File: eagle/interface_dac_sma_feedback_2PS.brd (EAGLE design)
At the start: 119.6 x 108.5 mm, 37 parts, among them K1 G5V-2, X4 BU-SMA-V

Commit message: feedback on hv rails
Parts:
- removed C3, C5, C6: (no value), resistor:C050-055X075
- removed C7: (no value), rcl:C050-030X075
- removed CONTROLGD1, POWERGD: (no value), con-molex:KK-156-2
- removed D1, D10, D4, D9: P6KEXXA, diode:C1702-15
- removed D11: 1N4148DO35-10, diode:DO35-10
- removed D14, D2, D5, D6: 4742, diode:ZDIO-10
- removed D7, D8: 1N4004, diode:DO41-10
- removed GND, HV1, LV1, OUT: TPPAD1-20Y, testpad:P1-20Y
- removed K1: G5V-2, relay:G5V-2
- removed R10, R11: 1M, rcl:0207/12
- removed U$3: UCC27425, texas:DIL08
- removed U$5: VP0550, transistor-fet:TO92-
- removed U$7: DA-2320, trafo:DIL06
- removed X4: BU-SMA-V, con-coax:BU-SMA-V
- added CONTROLGD2: (no value), con-molex:KK-156-2
- added CONTROLHV, FDBACKHV, POWERINTERFACE: (no value), con-molex:KK-156-3
- added IC1: ISO1540, texas:DIL08
- added OK1: PS2501", optocoupler:DIL16
- added PCB1: ARDUINO_MICRO, E14_Arduino_published:ARDUINO_MICRO
- added R1, R2: 1.5k, resistor:0207/12
- added R14: 1k, resistor:0207/12
- added R16: (no value), pot:SP19L
- added R18: 100, rcl:0207/12
- added R6: 10k, resistor:0207/12
- added T1, T2, T3, T4: TIP122V, transistor-npn:TO220V
- added X1: BU-SMA-V, con-coax:BU-SMA-V
- C1: device resistor:C050-055X075 -> rcl:C050-050X075
- C2: value (none) -> 10n; device resistor:C050-055X075 -> resistor:C050-024X044
- C4: device resistor:C050-055X075 -> resistor:C075-063X106
- R4: value 1M -> 1k; device rcl:0207/12 -> resistor:0207/12
- R7: value 1M -> 40k; device rcl:0207/12 -> resistor:0207/12
- U$1: value DA-2320 -> LTC6992; device trafo:DIL06 -> linear-technology:DIL06
- U$2: value VN0550 -> MCP4728DIL; device transistor-fet:TO92- -> microchip:DIL10
- U$4: value VP0550 -> MAX9650DIL; device transistor-fet:TO92- -> maxim:DIL06-4
- U$6: value VN0550 -> MAX9650DIL; device transistor-fet:TO92- -> maxim:DIL06-4
- moved R4 94.9 mm to (5.59, 99.3), turned to 270 degrees
- moved U$4 73.7 mm to (17.4, 93.7)
- moved C4 71.4 mm to (98.3, 62.4)
- moved U$6 65.1 mm to (83.1, 94.4), turned to 270 degrees
- moved U$2 56.1 mm to (42.4, 76.5), turned to 0 degrees
- moved U$1 36.1 mm to (88.1, 73.2), turned to 270 degrees
- moved R7 33.1 mm to (68.2, 74.4), turned to 0 degrees
- moved C1 31.2 mm to (34.8, 63.5), turned to 180 degrees
- moved C2 28.6 mm to (72.0, 64.1), turned to 180 degrees
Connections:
- removed net +15V: C7.1, D11.C, K1.1, K1.8, K1.9, POWERGD.1, U$3.6
- removed net ENSW: CONTROLGD1.1, D11.A, K1.16
- removed net N$10: D8.C, LV1.TP
- removed net N$11: C1.2, D2.A, U$5.2
- removed net N$22: C2.1, U$7.2
- removed net N$23: C6.1, U$7.3
- removed net N$25: C2.2, D6.C, U$2.2
- removed net N$27: C6.2, D14.C, U$6.2
- removed net N$29: D7.A, HV1.TP
- removed net N$30: D14.A, D4.A, D8.A, R11.1, U$6.3, U$7.4
- removed net N$6: C4.2, U$7.1
- removed net N$9: U$7.5
- new net +12V: POWERINTERFACE.1, T1.2, T2.2, T3.2, T4.2, U$4.6, U$6.6
- new net A+5: IC1.1, PCB1.+5V
- new net AGND: IC1.4, PCB1.GND., R18.2
- new net D10: PCB1.D10
- new net D11: PCB1.D11
- new net D4: PCB1.D4
- new net D7: PCB1.D7
- new net D8: PCB1.D8
- new net ENSW2: CONTROLGD2.1, OK1.16
- new net N$12: R16.E, U$1.SET
- new net N$19: R4.2, U$4.1
- new net N$8: FDBACKHV.1, U$4.4
- new net PWM5: PCB1.D5
- new net PWM6: PCB1.D6
- new net PWM9: OK1.1, PCB1.D9
- new net SCL: IC1.3, PCB1.D3
- new net SCL_OUT: IC1.6, R2.1, U$2.2
- new net SDA: IC1.2, PCB1.D2
- new net SDA_OUT: IC1.7, R1.1, U$2.3
- new net VCC: C1.1, C4.1, IC1.8, POWERINTERFACE.2, R1.2, R2.2, U$1.VCC, U$2.1
- net GND: now also C1.2, C2.2, C4.2, CONTROLGD2.2, CONTROLHV.2, FDBACKHV.2, IC1.5, OK1.15, POWERINTERFACE.3, R16.A, R16.S, R6.1, U$1.DIV, U$1.GND, U$2.10, U$2.4, U$4.2, U$6.2, X1.2, X1.3, X1.4, X1.5; no longer C7.2, CONTROLGD1.2, GND.TP, K1.11, K1.6, POWERGD.2, U$1.6, U$3.3, U$7.6, X4.2, X4.3, X4.4, X4.5
- net N$1: now also R7.1, U$2.6; no longer U$3.2, U$3.4, X4.1
- net N$13: now also U$1.OUT, X1.1; no longer D10.A, D4.C, D6.A, R10.1, R11.2, U$2.3, U$6.1
- net N$14: now also FDBACKHV.3, U$6.4; no longer K1.4, U$3.1
- net N$15: now also R14.1, T3.1, T4.1; no longer K1.13, U$3.8
- net N$16: now also U$2.9, U$4.3; no longer C5.2, D5.A, U$4.2
- net N$17: now also U$2.8; no longer D1.C, D5.C, D7.C, R4.2, U$1.4, U$4.3
- net N$18: now also U$2.7, U$6.3; no longer D1.A, D2.C, D9.C, R4.1, R7.2, U$1.5, U$4.1, U$5.3
- net N$2: now also C2.1, R6.2, R7.2, U$1.MOD; no longer C3.1, U$3.7
- net N$21: now also R14.2, U$6.1; no longer D10.C, D9.A, OUT.TP, R10.2, R7.1, U$2.1, U$5.1
- net N$3: now also R4.1, T1.1, T2.1; no longer C3.2, U$1.1
- net N$4: now also CONTROLHV.1, T1.3, T2.3; no longer C4.1, U$3.5
- net N$5: now also CONTROLHV.3, T3.3, T4.3; no longer C1.1, U$1.2
- net N$7: now also OK1.2, R18.1; no longer C5.1, U$1.3
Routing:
- net VCC: track 0.00 -> 162.9 mm
- net +12V: track 0.00 -> 149.3 mm
- net N$17: track 85.6 -> 0.00 mm
- net N$30: track 83.5 -> 0.00 mm, vias 2 -> 0
- net +15V: track 77.9 -> 0.00 mm
- net GND: track 115.7 -> 48.1 mm, vias 2 -> 0
- net AGND: track 0.00 -> 63.8 mm
- net A+5: track 0.00 -> 51.8 mm
- net N$18: track 90.7 -> 40.6 mm
- net N$13: track 55.6 -> 8.72 mm
- net SCL_OUT: track 0.00 -> 46.8 mm, vias 0 -> 2
- net SDA_OUT: track 0.00 -> 36.5 mm
- net N$4: track 12.3 -> 47.7 mm
- net N$9: track 35.3 -> 0.00 mm
- net SDA: track 0.00 -> 34.0 mm
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- added copper zone on layer 16, net AGND
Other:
- board size 119.6 x 108.5 mm -> 109.5 x 133.3 mm

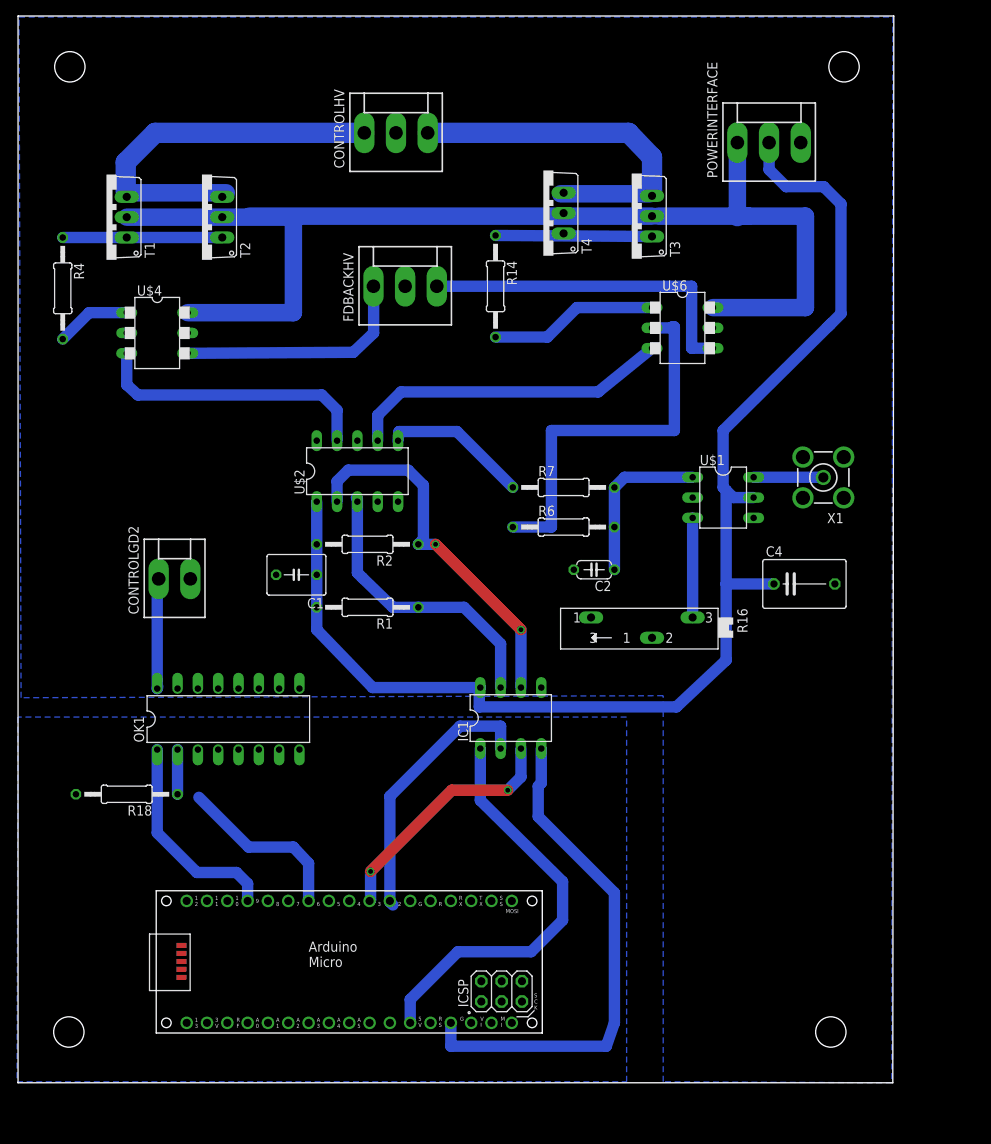
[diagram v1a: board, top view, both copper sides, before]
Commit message: 3PS, 2 1kV in parallel
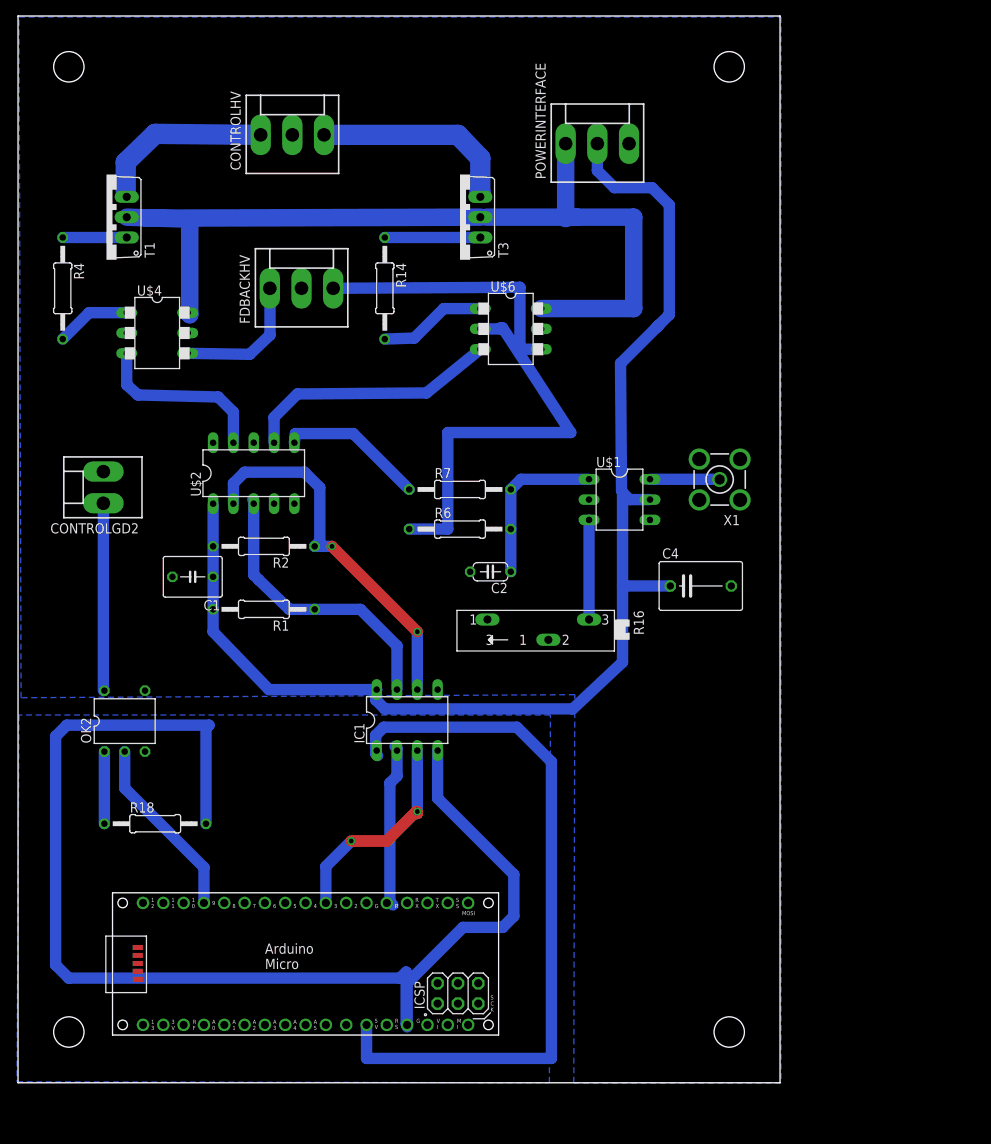
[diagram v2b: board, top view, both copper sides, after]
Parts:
- removed OK1: PS2501", optocoupler:DIL16
- removed T2, T4: TIP122V, transistor-npn:TO220V
- added OK2: H11F1, optocoupler:DIL05
- moved U$6 21.5 mm to (61.6, 94.2)
- moved T3 21.5 mm to (55.2, 108.2)
- moved POWERINTERFACE 21.5 mm to (72.4, 117.4)
- moved CONTROLGD2 14.5 mm to (10.7, 74.4), turned to 90 degrees
- moved R14 13.8 mm to (45.8, 99.3)
- moved C4 13.0 mm to (85.3, 62.1)
- moved R16 13.0 mm to (64.4, 56.6)
- moved U$1 13.0 mm to (75.2, 72.9)
- moved X1 13.0 mm to (87.7, 75.4)
- moved C1 13.0 mm to (21.8, 63.2)
- moved C2 13.0 mm to (59.1, 63.9)
- moved CONTROLHV 13.0 mm to (34.3, 118.5)
- moved FDBACKHV 13.0 mm to (35.4, 99.3)
- moved IC1 13.0 mm to (48.6, 45.3)
- moved R1 13.0 mm to (30.7, 59.2)
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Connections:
- net +12V: no longer T2.2, T4.2
- net ENSW2: now also OK2.6; no longer OK1.16
- net GND: now also OK2.4; no longer OK1.15
- net N$15: no longer T4.1
- net N$3: no longer T2.1
- net N$4: no longer T2.3
- net N$5: no longer T4.3
- net N$7: now also OK2.1; no longer OK1.2
- net PWM9: now also OK2.2; no longer OK1.1
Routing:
- net AGND: track 63.8 -> 159.2 mm
- net A+5: track 51.8 -> 91.2 mm
- net +12V: track 149.3 -> 115.0 mm
- net N$4: track 47.7 -> 22.2 mm
- net PWM6: track 21.9 -> 0.00 mm
- net N$5: track 45.1 -> 25.3 mm
- net SDA: track 34.0 -> 20.4 mm
- net N$8: track 30.0 -> 17.1 mm
- net N$16: track 35.3 -> 22.4 mm
- net N$3: track 19.9 -> 8.00 mm
- net ENSW2: track 14.8 -> 23.4 mm
- net N$14: track 42.3 -> 33.8 mm
- net N$18: track 40.6 -> 32.1 mm
- net N$15: track 19.6 -> 11.9 mm
- net N$21: track 21.1 -> 13.5 mm
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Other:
- board size 109.5 x 133.3 mm -> 95.2 x 133.3 mm

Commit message: IXYS board solution, gatedriver components
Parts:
- moved C4 5.21 mm to (81.8, 58.3), turned to 270 degrees
- moved X1 3.94 mm to (83.8, 75.4)
- moved POWERINTERFACE 3.19 mm to (69.2, 117.1)
- moved R16 2.69 mm to (61.7, 56.3)
- moved U$1 2.67 mm to (72.5, 72.9)
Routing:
- net +12V: track 115.0 -> 84.8 mm
- net GND: track 50.8 -> 38.7 mm
- net VCC: track 158.6 -> 152.1 mm
- net N$2: track 20.6 -> 17.9 mm
- net N$13: track 8.72 -> 7.44 mm
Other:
- board size 95.2 x 133.3 mm -> 89.9 x 133.3 mm

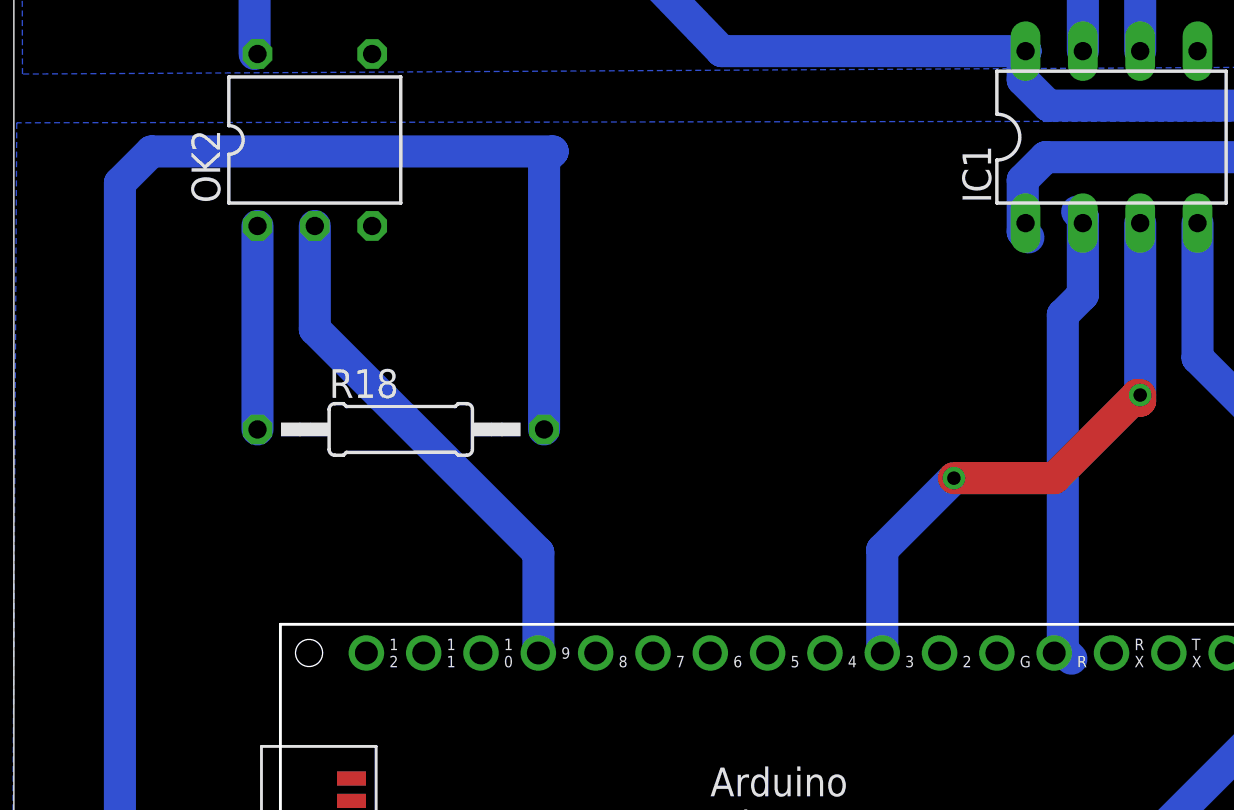
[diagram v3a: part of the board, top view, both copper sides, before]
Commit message: layout fixes
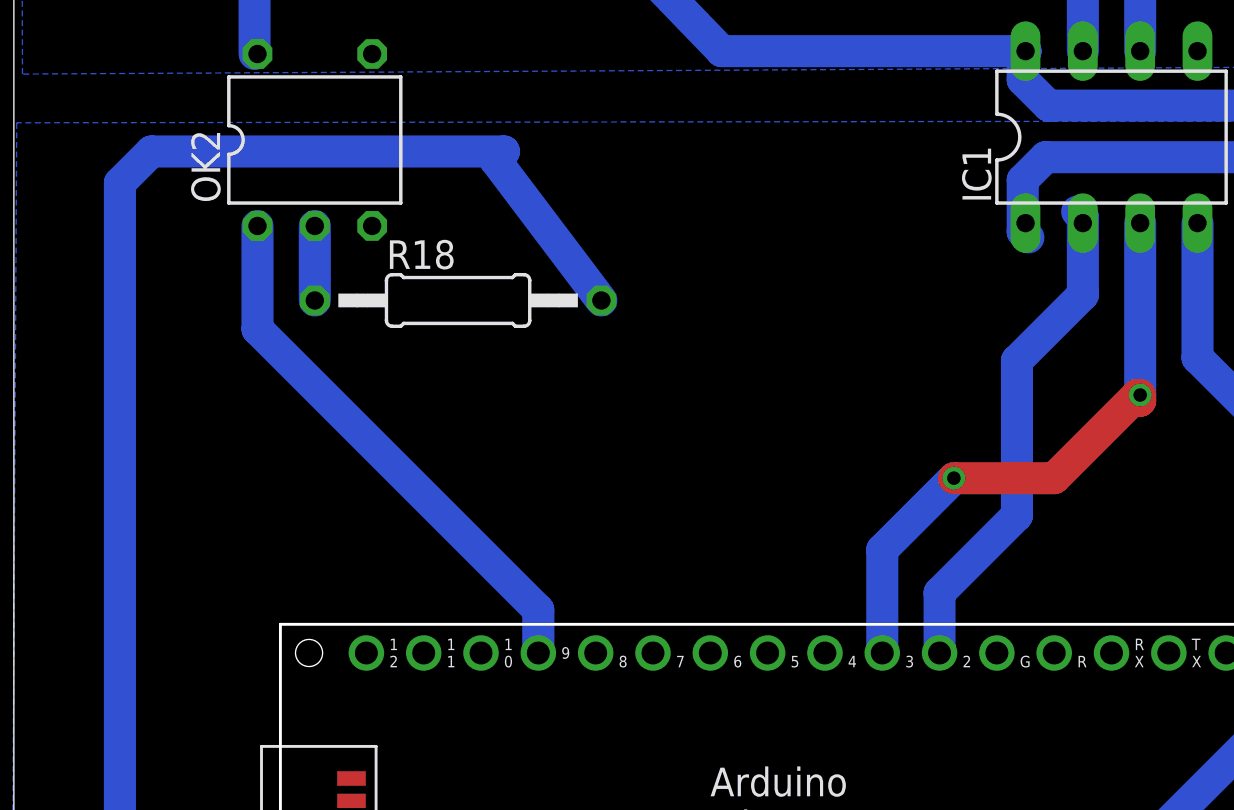
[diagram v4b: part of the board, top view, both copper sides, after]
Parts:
- moved R18 6.25 mm to (19.7, 38.1)
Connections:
- removed net N$7: OK2.1, R18.1
- new net N$6: OK2.2, R18.1
- net PWM9: now also OK2.1; no longer OK2.2
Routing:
- net N$7: track 9.02 -> 0.00 mm
- net AGND: track 159.2 -> 152.9 mm
- net N$6: track 0.00 -> 3.30 mm
- net SDA: track 20.4 -> 22.3 mm
- net PWM9: track 23.0 -> 24.1 mm
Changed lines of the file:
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@@
 <attribute name="OC_FARNELL" value="unknown" x="83.7692" y="75.4126" size="1.778" layer="27" rot="R180" display="off"/>
 </element>
-<element name="R18" library="rcl" package="0207/12" value="100" x="17.145" y="32.385"/>
+<element name="R18" library="rcl" package="0207/12" value="100" x="19.685" y="38.1"/>
 <element name="CONTROLGD2" library="con-molex" package="KK-156-2" value="" x="10.668" y="74.422" rot="R90">
 <attribute name="OC_NEWARK" value="unknown" x="10.668" y="74.422" size="1.778" layer="27" rot="R90" display="off"/>
@@
 <wire x1="48.641" y1="12.446" x2="48.641" y2="7.239" width="1.4224" layer="16"/>
 <wire x1="48.641" y1="7.239" x2="48.641" y2="6.985" width="1.4224" layer="16"/>
-<wire x1="23.495" y1="32.385" x2="23.495" y2="44.323" width="1.4224" layer="16"/>
-<wire x1="23.495" y1="44.323" x2="23.876" y2="44.704" width="1.4224" layer="16"/>
-<wire x1="23.876" y1="44.704" x2="6.096" y2="44.704" width="1.4224" layer="16"/>
+<wire x1="26.035" y1="38.1" x2="21.336" y2="44.323" width="1.4224" layer="16"/>
+<wire x1="21.336" y1="44.323" x2="21.717" y2="44.704" width="1.4224" layer="16"/>
+<wire x1="21.717" y1="44.704" x2="6.096" y2="44.704" width="1.4224" layer="16"/>
 <wire x1="6.096" y1="44.704" x2="4.699" y2="43.307" width="1.4224" layer="16"/>
 <wire x1="4.699" y1="43.307" x2="4.699" y2="14.732" width="1.4224" layer="16"/>
@@
 <contactref element="PCB1" pad="D2"/>
 <contactref element="IC1" pad="2"/>
-<wire x1="46.482" y1="37.465" x2="46.482" y2="22.606" width="1.4224" layer="16"/>
-<wire x1="46.482" y1="22.606" x2="46.863" y2="22.225" width="1.4224" layer="16"/>
-<wire x1="46.482" y1="37.465" x2="47.371" y2="38.354" width="1.4224" layer="16"/>
+<wire x1="44.45" y1="35.433" x2="44.45" y2="28.575" width="1.4224" layer="16"/>
+<wire x1="44.45" y1="35.433" x2="47.371" y2="38.354" width="1.4224" layer="16"/>
 <wire x1="47.371" y1="38.354" x2="47.371" y2="41.783" width="1.4224" layer="16"/>
 <wire x1="47.371" y1="41.783" x2="47.117" y2="42.037" width="1.4224" layer="16"/>
+<wire x1="44.45" y1="28.575" x2="41.021" y2="25.146" width="1.4224" layer="16"/>
+<wire x1="41.021" y1="25.146" x2="41.021" y2="22.479" width="1.4224" layer="16"/>
 <wire x1="47.371" y1="41.783" x2="47.371" y2="41.529" width="0" layer="19" extent="16-16"/>
-<wire x1="41.021" y1="22.479" x2="46.482" y2="22.606" width="0" layer="19" extent="16-16"/>
 </signal>
 <signal name="PWM9">
 <contactref element="PCB1" pad="D9"/>
-<contactref element="OK2" pad="2"/>
-<wire x1="13.335" y1="41.402" x2="13.335" y2="36.83" width="1.4224" layer="16"/>
-<wire x1="13.335" y1="36.83" x2="23.241" y2="26.924" width="1.4224" layer="16"/>
-<wire x1="23.241" y1="26.924" x2="23.241" y2="22.479" width="1.4224" layer="16"/>
+<wire x1="10.795" y1="36.83" x2="23.241" y2="24.384" width="1.4224" layer="16"/>
+<wire x1="23.241" y1="24.384" x2="23.241" y2="22.479" width="1.4224" layer="16"/>
+<contactref element="OK2" pad="1"/>
+<wire x1="10.795" y1="41.402" x2="10.795" y2="36.83" width="1.4224" layer="16"/>
 </signal>
 <signal name="N$12">
@@
 <wire x1="76.327" y1="75.438" x2="83.4898" y2="75.438" width="1.4224" layer="16"/>
 <wire x1="83.4898" y1="75.438" x2="83.7692" y2="75.4126" width="1.4224" layer="16"/>
-</signal>
-<signal name="N$7">
-<contactref element="R18" pad="1"/>
-<contactref element="OK2" pad="1"/>
-<wire x1="10.795" y1="41.402" x2="10.795" y2="32.385" width="1.4224" layer="16"/>
 </signal>
 <signal name="ENSW2">
@@
 <wire x1="5.588" y1="105.664" x2="13.589" y2="105.664" width="1.4224" layer="16"/>
 </signal>
+<signal name="N$6">
+<contactref element="OK2" pad="2"/>
+<contactref element="R18" pad="1"/>
+<wire x1="13.335" y1="38.1" x2="13.335" y2="41.402" width="1.4224" layer="16"/>
+</signal>
 </signals>
